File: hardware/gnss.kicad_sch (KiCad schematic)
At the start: 8 parts, among them U1 SAM-M10Q

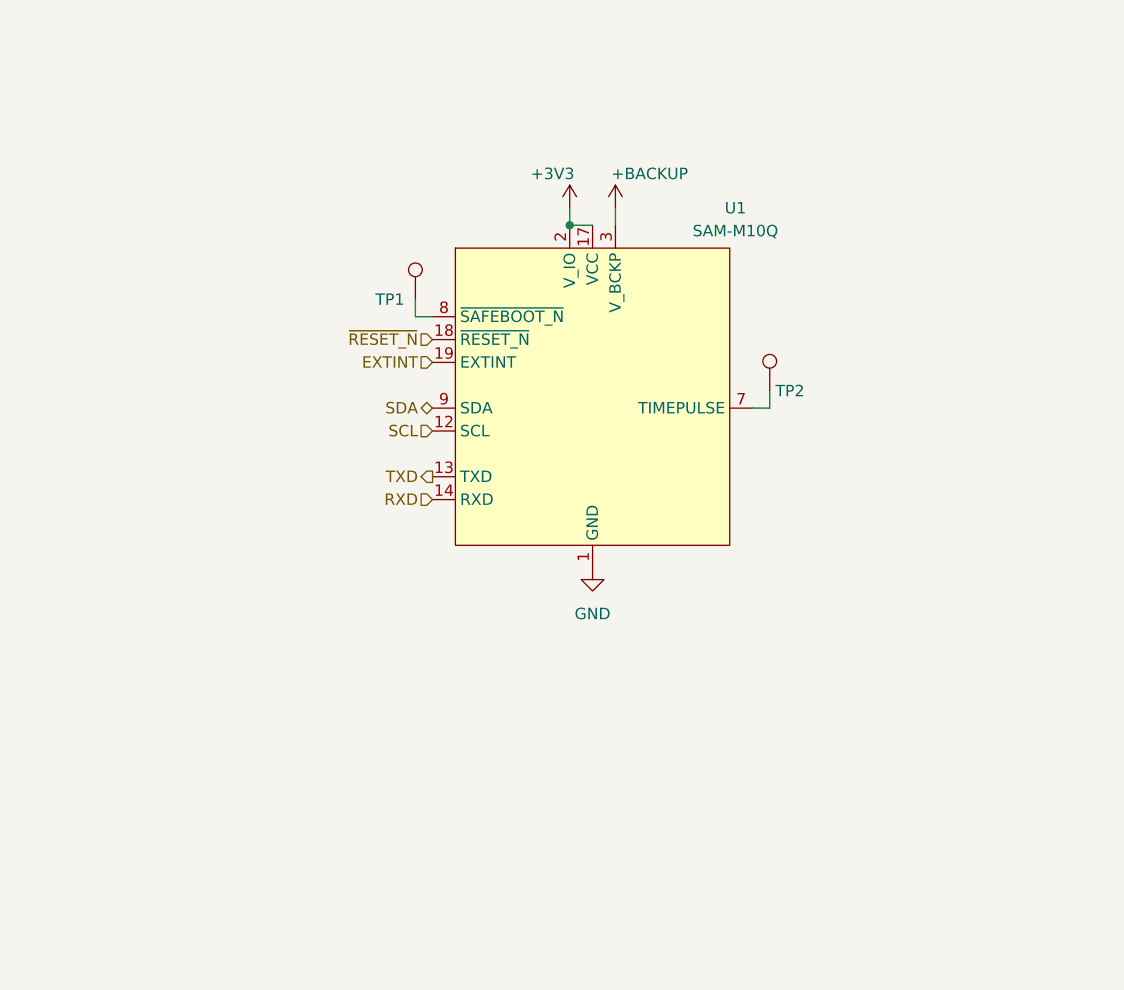
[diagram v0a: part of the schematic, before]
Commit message: drew more busses and connections
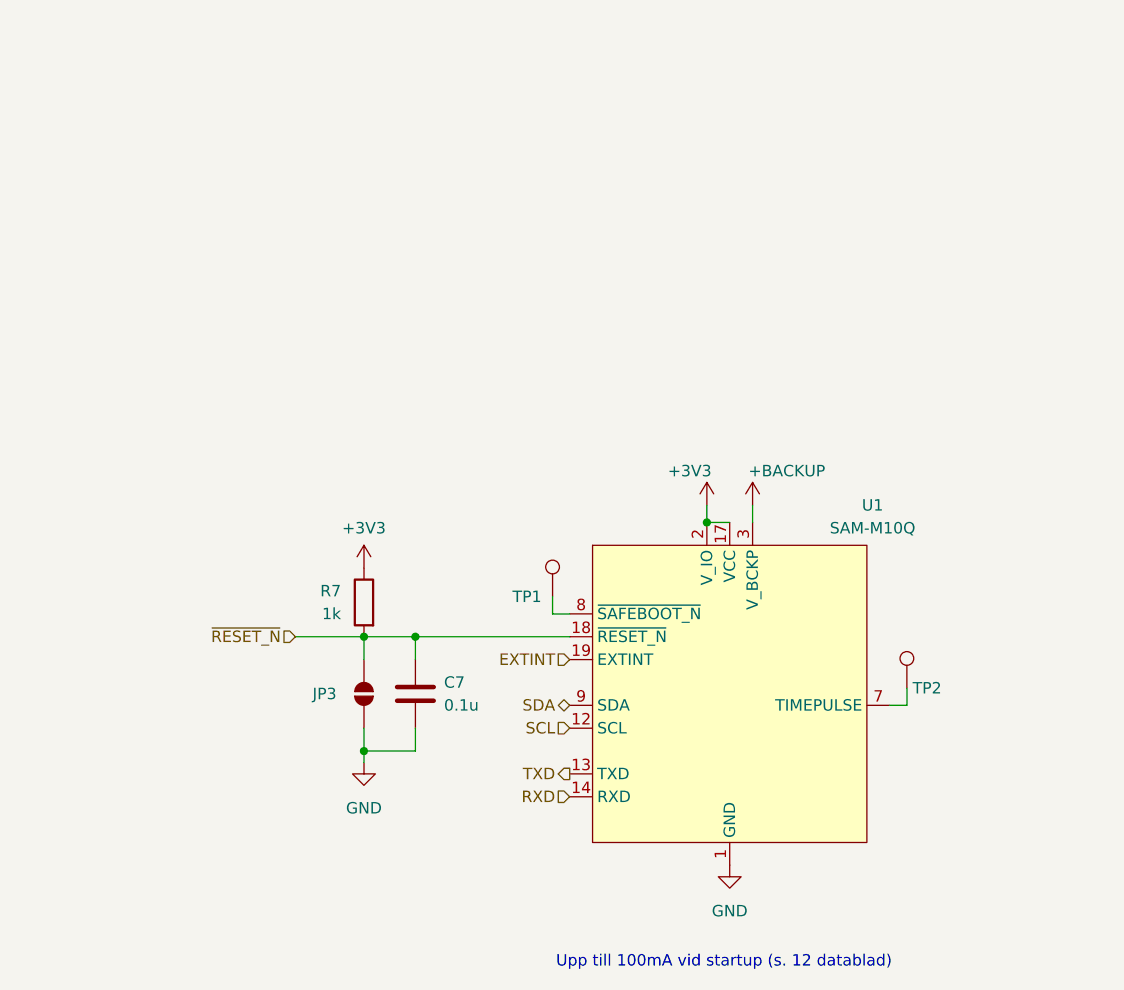
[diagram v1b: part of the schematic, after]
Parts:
- added C7: 0.1u, symbol Device:C
- added JP3: SolderJumper_2_Open, symbol Jumper:SolderJumper_2_Open
- added R7: 1k, symbol Device:R
- U1: Integration Manual (none) -> https://content.u-blox.com/sites/default/files/documents/SA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
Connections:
- net +3V3: now also R7.1
- net GND: now also C7.2, JP3.2 (B)
- net ~{RESET_N}: now also C7.1, JP3.1 (A), R7.2
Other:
- note added: "Upp till 100mA vid startup (s. 12 datablad)"
- moved on the sheet: TP1, TP2, U1
